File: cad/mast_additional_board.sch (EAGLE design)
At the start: 22 parts, among them K1 CPC1002N, K2 CPC1002N

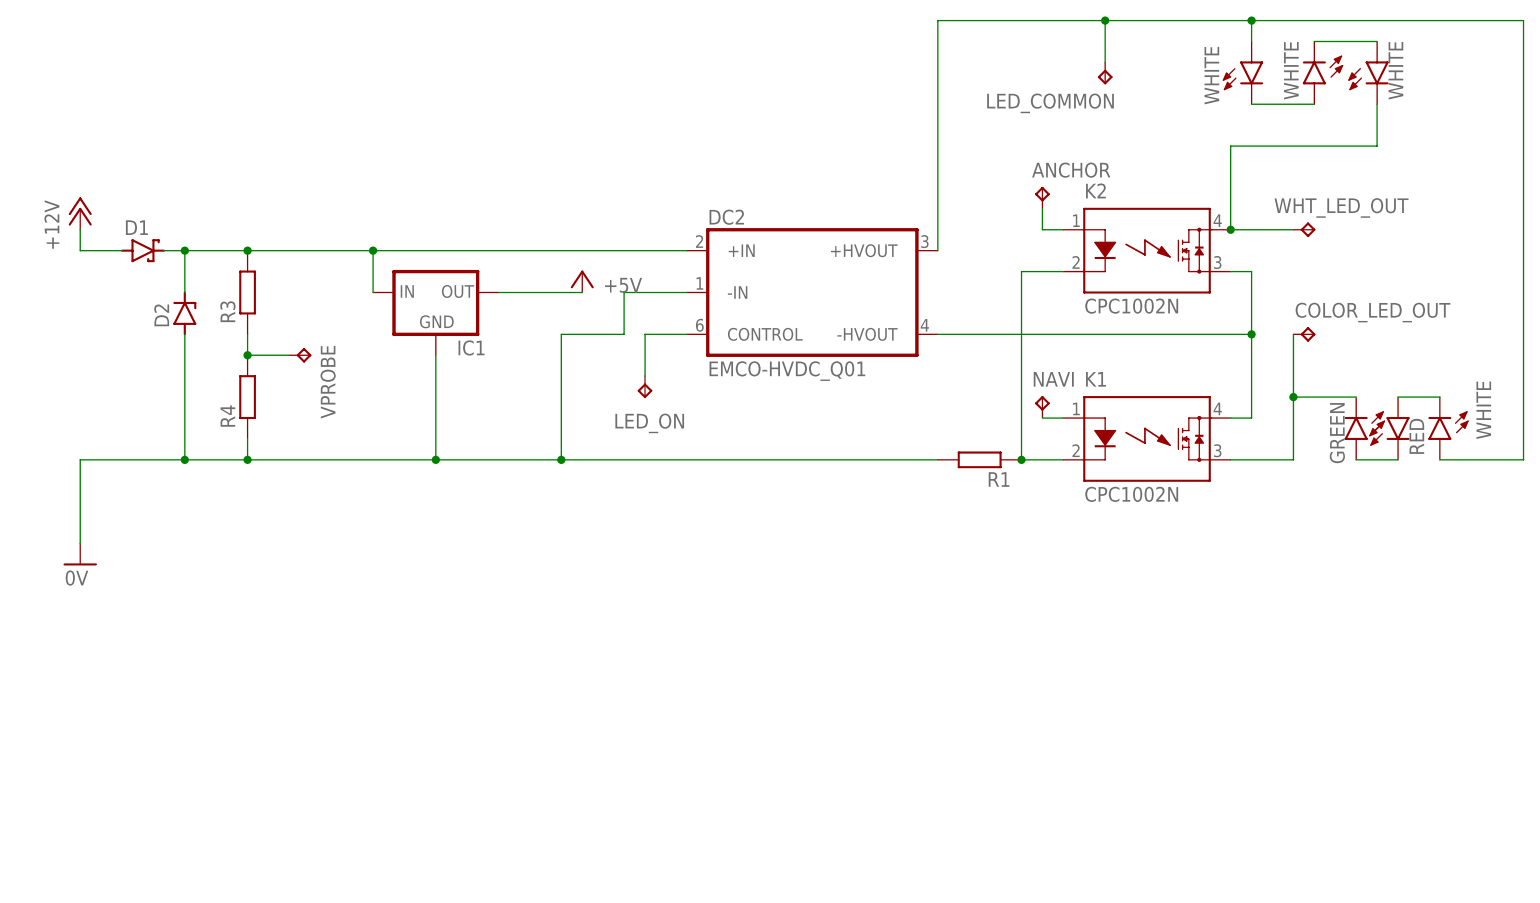
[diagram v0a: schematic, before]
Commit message: Additional top mast module
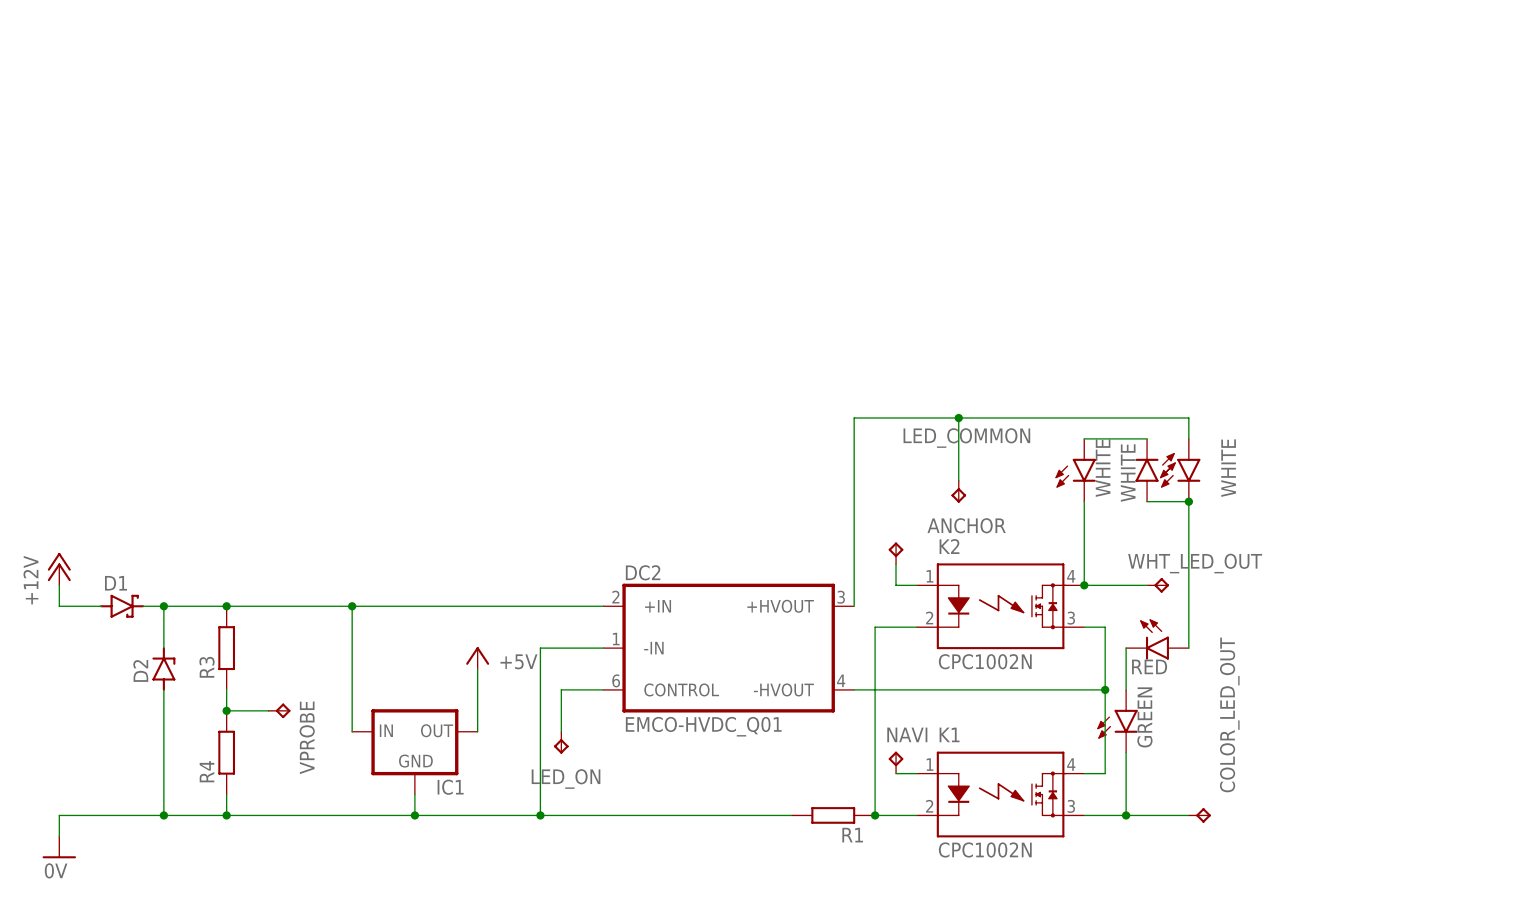
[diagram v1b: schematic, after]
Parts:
- removed LED4: WHITE, led:LED5MM
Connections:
- removed net N$13: LED4.C, LED5.A
- net N$15: no longer LED4.A
- net N$8: now also LED5.A
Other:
- moved on the sheet: ANCHOR, COLOR_LED_OUT, D1, D2, DC2, IC1, K1, K2, LED_COMMON, LED_ON, NAVI, R1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
